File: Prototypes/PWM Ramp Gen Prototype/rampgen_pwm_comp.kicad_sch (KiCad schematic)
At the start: 11 parts, among them U7 TLV3502

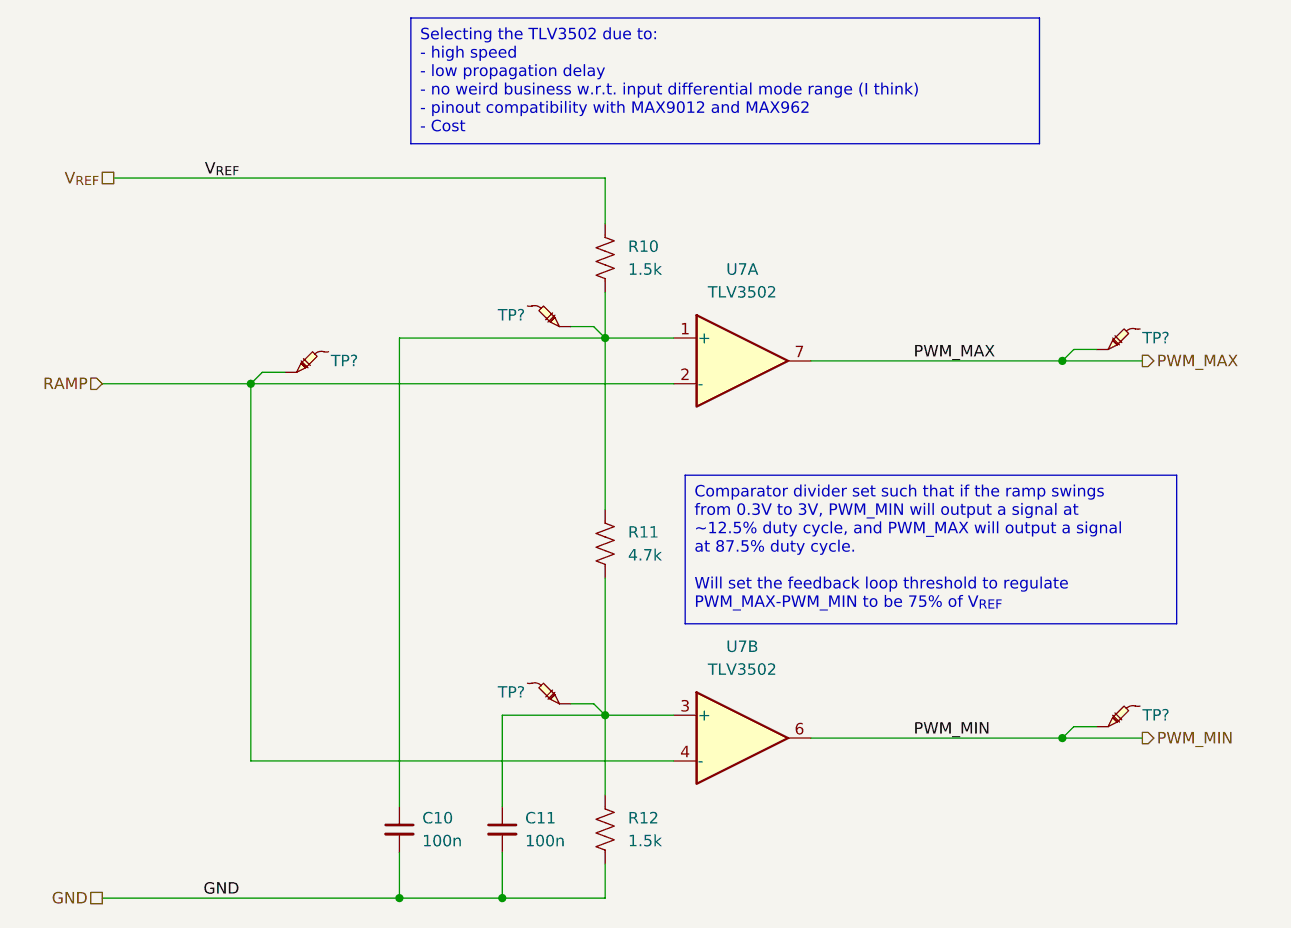
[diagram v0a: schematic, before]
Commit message: Comparator and Op-amp tweaks for BOM consolidation; final layout
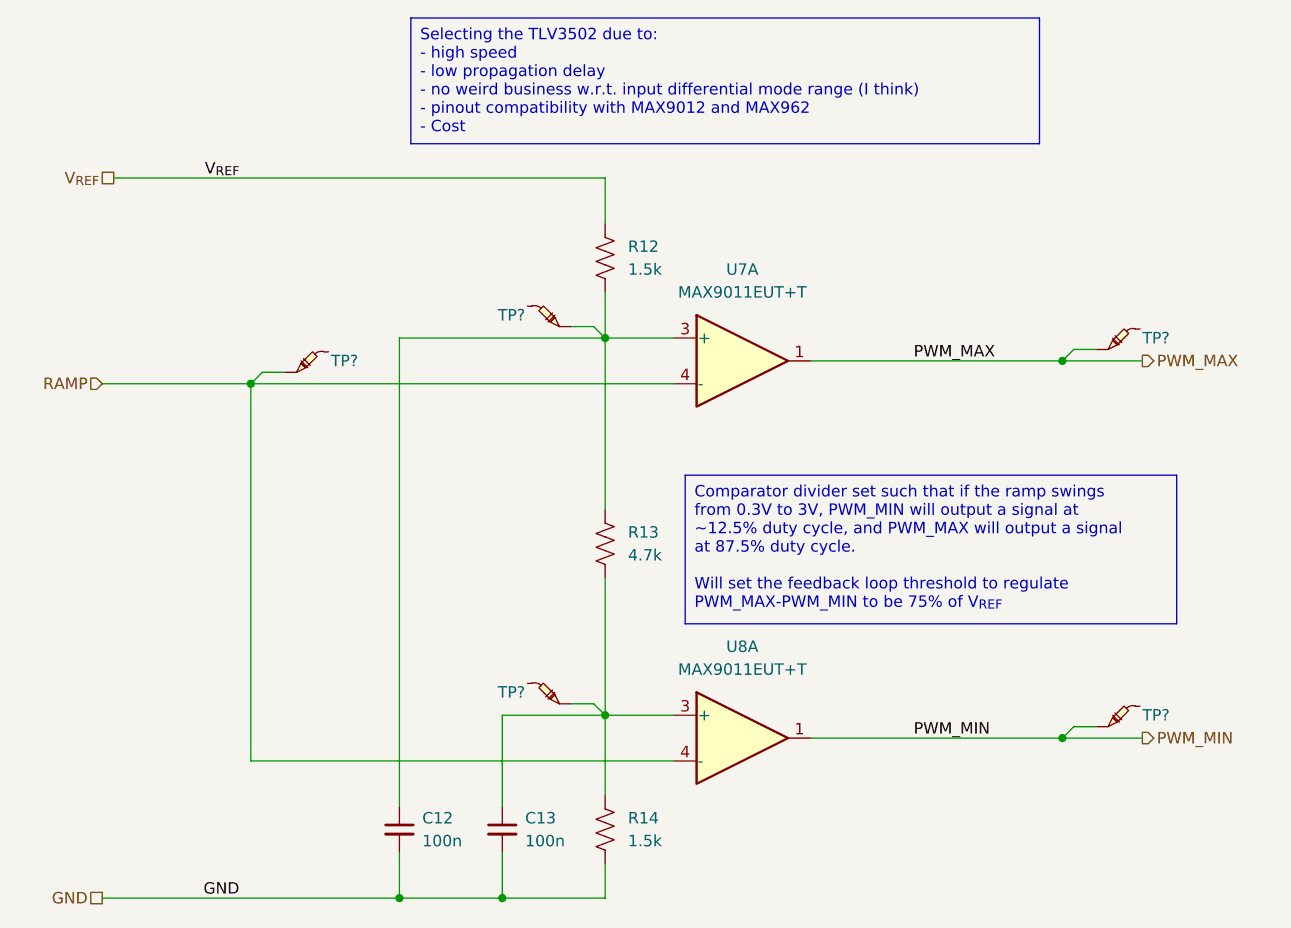
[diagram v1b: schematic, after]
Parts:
- removed U7: TLV3502, Package_SO:SOIC-8_3.9x4.9mm_P1.27mm, symbol Custom-AnalogIC:TLV3502
- added U7, U8: MAX9011EUT+T, Package_TO_SOT_SMD:SOT-23-6_Handsoldering, symbol Custom-AnalogIC:MAX9011
- renumbered C10 to C12, C11 to C13, R10 to R12, R11 to R13, R12 to R14
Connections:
- net PWM_MAX: now also U7.1
- net PWM_MIN: now also U8.1
- net RAMP: now also U7.4 (-), U8.4 (-)
- net at C12.1, R12.2, R13.1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: now also U7.3 (+)
- net at C13.1, R13.2, R14.1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: now also U8.3 (+)
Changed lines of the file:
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@@
         )
         (path "/a1dfcc81-abac-4d0f-af30-e0b6fd53034d/f61e0f34-ca28-4cd6-9cf5-9004e61b4706"
-          (reference "TP19") (unit 1)
-        )
-      )
-    )
-  )
-  (symbol (lib_id "Custom-AnalogIC:TLV3502") (at 153.67 120.65 0) (unit 2)
-    (in_bom yes) (on_board yes) (dnp no) (fields_autoplaced)
-    (property "Reference" "U7" (at 153.67 110.49 0)
+          (reference "TP17") (unit 1)
+        )
+      )
+    )
+  )
+  (symbol (lib_id "Custom-AnalogIC:MAX9011") (at 153.67 120.65 0) (unit 1)
+    (in_bom yes) (on_board yes) (dnp no) (fields_autoplaced)
+    (property "Reference" "U8" (at 153.67 110.49 0)
       (effects (font (size 1.27 1.27)))
     )
-    (property "Value" "TLV3502" (at 153.67 113.03 0)
+    (property "Value" "MAX9011EUT+T" (at 153.67 113.03 0)
       (effects (font (size 1.27 1.27)))
     )
-    (property "Footprint" "Package_SO:SOIC-8_3.9x4.9mm_P1.27mm" (at 153.67 120.65 0)
-      (effects (font (size 1.27 1.27)) hide)
-    )
-    (property "Datasheet" "https://www.ti.com/lit/ds/symlink/tlv3501.pdf" (at 153.67 120.65 0)
-      (effects (font (size 1.27 1.27)) hide)
-    )
-    (property "Manufacturer" "Texas Instruments" (at 153.67 120.65 0)
-      (effects (font (size 1.27 1.27)) hide)
-    )
-    (property "Part Number" "TLV3502AIDR" (at 153.67 120.65 0)
-      (effects (font (size 1.27 1.27)) hide)
-    )
-    (pin "1")
-    (pin "2")
-    (pin "7")
+    (property "Footprint" "Package_TO_SOT_SMD:SOT-23-6_Handsoldering" (at 153.67 120.65 0)
+      (effects (font (size 1.27 1.27)) hide)
+    )
+    (property "Datasheet" "https://datasheets.maximintegrated.com/en/ds/MAX9010-MAX9013.pdf" (at 153.67 120.65 0)
+      (effects (font (size 1.27 1.27)) hide)
+    )
+    (property "Manufacturer" "Analog Devices Inc./Maxim Integrated" (at 153.67 120.65 0)
+      (effects (font (size 1.27 1.27)) hide)
+    )
+    (property "Part Number" "MAX9011EUT+T" (at 153.67 120.65 0)
+      (effects (font (size 1.27 1.27)) hide)
+    )
+    (pin "1")
     (pin "3")
     (pin "4")
+    (pin "2")
+    (pin "5")
     (pin "6")
-    (pin "5")
-    (pin "8")
-    (instances
-      (project "PWM Ramp Gen Prototype"
-        (path "/a1dfcc81-abac-4d0f-af30-e0b6fd53034d/f61e0f34-ca28-4cd6-9cf5-9004e61b4706"
-          (reference "U7") (unit 2)
+    (instances
+      (project "PWM Ramp Gen Prototype"
+        (path "/a1dfcc81-abac-4d0f-af30-e0b6fd53034d/f61e0f34-ca28-4cd6-9cf5-9004e61b4706"
+          (reference "U8") (unit 1)
         )
       )
@@
         )
         (path "/a1dfcc81-abac-4d0f-af30-e0b6fd53034d/f61e0f34-ca28-4cd6-9cf5-9004e61b4706"
-          (reference "TP22") (unit 1)
+          (reference "TP20") (unit 1)
         )
       )
@@
         )
         (path "/a1dfcc81-abac-4d0f-af30-e0b6fd53034d/f61e0f34-ca28-4cd6-9cf5-9004e61b4706"
-          (reference "TP21") (unit 1)
+          (reference "TP19") (unit 1)
         )
       )
@@
   (symbol (lib_id "Custom-Resistor:RMCF0603FT4K70") (at 138.43 99.06 0) (unit 1)
     (in_bom yes) (on_board yes) (dnp no) (fields_autoplaced)
-    (property "Reference" "R11" (at 140.97 97.79 0)
+    (property "Reference" "R13" (at 140.97 97.79 0)
       (effects (font (size 1.27 1.27)) (justify left))
     )
@@
       (project "PWM Ramp Gen Prototype"
         (path "/a1dfcc81-abac-4d0f-af30-e0b6fd53034d/f61e0f34-ca28-4cd6-9cf5-9004e61b4706"
-          (reference "R11") (unit 1)
+          (reference "R13") (unit 1)
+        )
+      )
+    )
+  )
+  (symbol (lib_id "Custom-AnalogIC:MAX9011") (at 153.67 78.74 0) (unit 1)
+    (in_bom yes) (on_board yes) (dnp no) (fields_autoplaced)
+    (property "Reference" "U7" (at 153.67 68.58 0)
+      (effects (font (size 1.27 1.27)))
+    )
+    (property "Value" "MAX9011EUT+T" (at 153.67 71.12 0)
+      (effects (font (size 1.27 1.27)))
+    )
+    (property "Footprint" "Package_TO_SOT_SMD:SOT-23-6_Handsoldering" (at 153.67 78.74 0)
+      (effects (font (size 1.27 1.27)) hide)
+    )
+    (property "Datasheet" "https://datasheets.maximintegrated.com/en/ds/MAX9010-MAX9013.pdf" (at 153.67 78.74 0)
+      (effects (font (size 1.27 1.27)) hide)
+    )
+    (property "Manufacturer" "Analog Devices Inc./Maxim Integrated" (at 153.67 78.74 0)
+      (effects (font (size 1.27 1.27)) hide)
+    )
+    (property "Part Number" "MAX9011EUT+T" (at 153.67 78.74 0)
+      (effects (font (size 1.27 1.27)) hide)
+    )
+    (pin "1")
+    (pin "3")
+    (pin "4")
+    (pin "2")
+    (pin "5")
+    (pin "6")
+    (instances
+      (project "PWM Ramp Gen Prototype"
+        (path "/a1dfcc81-abac-4d0f-af30-e0b6fd53034d/f61e0f34-ca28-4cd6-9cf5-9004e61b4706"
+          (reference "U7") (unit 1)
         )
       )
@@
   (symbol (lib_id "Custom-Capacitor:CL10B104KB8NNWC") (at 127 130.81 0) (unit 1)
     (in_bom yes) (on_board yes) (dnp no) (fields_autoplaced)
-    (property "Reference" "C11" (at 129.54 129.5463 0)
+    (property "Reference" "C13" (at 129.54 129.5463 0)
       (effects (font (size 1.27 1.27)) (justify left))
     )
@@
       (project "PWM Ramp Gen Prototype"
         (path "/a1dfcc81-abac-4d0f-af30-e0b6fd53034d/f61e0f34-ca28-4cd6-9cf5-9004e61b4706"
-          (reference "C11") (unit 1)
+          (reference "C13") (unit 1)
         )
       )
@@
         )
         (path "/a1dfcc81-abac-4d0f-af30-e0b6fd53034d/f61e0f34-ca28-4cd6-9cf5-9004e61b4706"
-          (reference "TP18") (unit 1)
-        )
-      )
-    )
-  )
-  (symbol (lib_id "Custom-AnalogIC:TLV3502") (at 153.67 78.74 0) (unit 1)
-    (in_bom yes) (on_board yes) (dnp no) (fields_autoplaced)
-    (property "Reference" "U7" (at 153.67 68.58 0)
-      (effects (font (size 1.27 1.27)))
-    )
-    (property "Value" "TLV3502" (at 153.67 71.12 0)
-      (effects (font (size 1.27 1.27)))
-    )
-    (property "Footprint" "Package_SO:SOIC-8_3.9x4.9mm_P1.27mm" (at 153.67 78.74 0)
-      (effects (font (size 1.27 1.27)) hide)
-    )
-    (property "Datasheet" "https://www.ti.com/lit/ds/symlink/tlv3501.pdf" (at 153.67 78.74 0)
-      (effects (font (size 1.27 1.27)) hide)
-    )
-    (property "Manufacturer" "Texas Instruments" (at 153.67 78.74 0)
-      (effects (font (size 1.27 1.27)) hide)
-    )
-    (property "Part Number" "TLV3502AIDR" (at 153.67 78.74 0)
-      (effects (font (size 1.27 1.27)) hide)
-    )
-    (pin "1")
-    (pin "2")
-    (pin "7")
-    (pin "3")
-    (pin "4")
-    (pin "6")
-    (pin "5")
-    (pin "8")
-    (instances
-      (project "PWM Ramp Gen Prototype"
-        (path "/a1dfcc81-abac-4d0f-af30-e0b6fd53034d/f61e0f34-ca28-4cd6-9cf5-9004e61b4706"
-          (reference "U7") (unit 1)
+          (reference "TP16") (unit 1)
         )
       )
@@
   (symbol (lib_id "Custom-Capacitor:CL10B104KB8NNWC") (at 115.57 130.81 0) (unit 1)
     (in_bom yes) (on_board yes) (dnp no) (fields_autoplaced)
-    (property "Reference" "C10" (at 118.11 129.5463 0)
+    (property "Reference" "C12" (at 118.11 129.5463 0)
       (effects (font (size 1.27 1.27)) (justify left))
     )
@@
       (project "PWM Ramp Gen Prototype"
         (path "/a1dfcc81-abac-4d0f-af30-e0b6fd53034d/f61e0f34-ca28-4cd6-9cf5-9004e61b4706"
-          (reference "C10") (unit 1)
+          (reference "C12") (unit 1)
         )
       )
@@
         )
         (path "/a1dfcc81-abac-4d0f-af30-e0b6fd53034d/f61e0f34-ca28-4cd6-9cf5-9004e61b4706"
-          (reference "TP20") (unit 1)
+          (reference "TP18") (unit 1)
         )
       )
@@
   (symbol (lib_id "Custom-Resistor:RMCF0603FT1K50") (at 138.43 130.81 0) (unit 1)
     (in_bom yes) (on_board yes) (dnp no)
-    (property "Reference" "R12" (at 140.97 129.54 0)
+    (property "Reference" "R14" (at 140.97 129.54 0)
       (effects (font (size 1.27 1.27)) (justify left))
     )
@@
       (project "PWM Ramp Gen Prototype"
         (path "/a1dfcc81-abac-4d0f-af30-e0b6fd53034d/f61e0f34-ca28-4cd6-9cf5-9004e61b4706"
-          (reference "R12") (unit 1)
+          (reference "R14") (unit 1)
         )
       )
@@
   (symbol (lib_id "Custom-Resistor:RMCF0603FT1K50") (at 138.43 67.31 0) (unit 1)
     (in_bom yes) (on_board yes) (dnp no)
-    (property "Reference" "R10" (at 140.97 66.04 0)
+    (property "Reference" "R12" (at 140.97 66.04 0)
       (effects (font (size 1.27 1.27)) (justify left))
     )
@@
       (project "PWM Ramp Gen Prototype"
         (path "/a1dfcc81-abac-4d0f-af30-e0b6fd53034d/f61e0f34-ca28-4cd6-9cf5-9004e61b4706"
-          (reference "R10") (unit 1)
-        )
-      )
+          (reference "R12") (unit 1)
+        )
+      )
